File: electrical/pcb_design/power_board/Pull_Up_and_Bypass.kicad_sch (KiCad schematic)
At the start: 22 parts

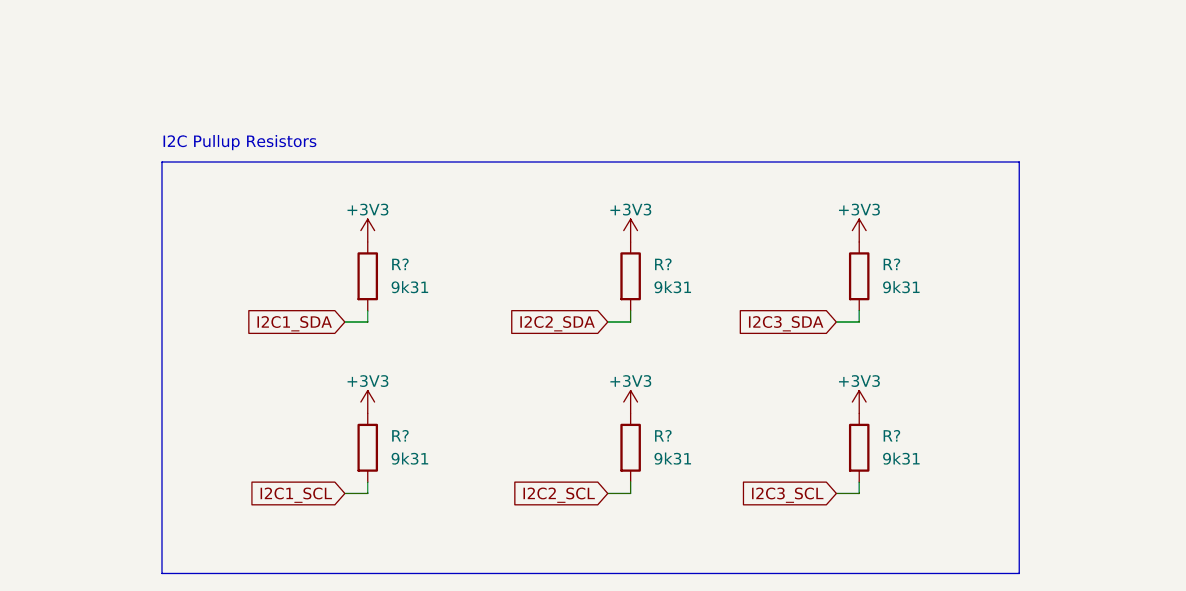
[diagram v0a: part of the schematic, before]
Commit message: power board schematic first draft but missing some resistor and diode specs, and smart mcu pinout
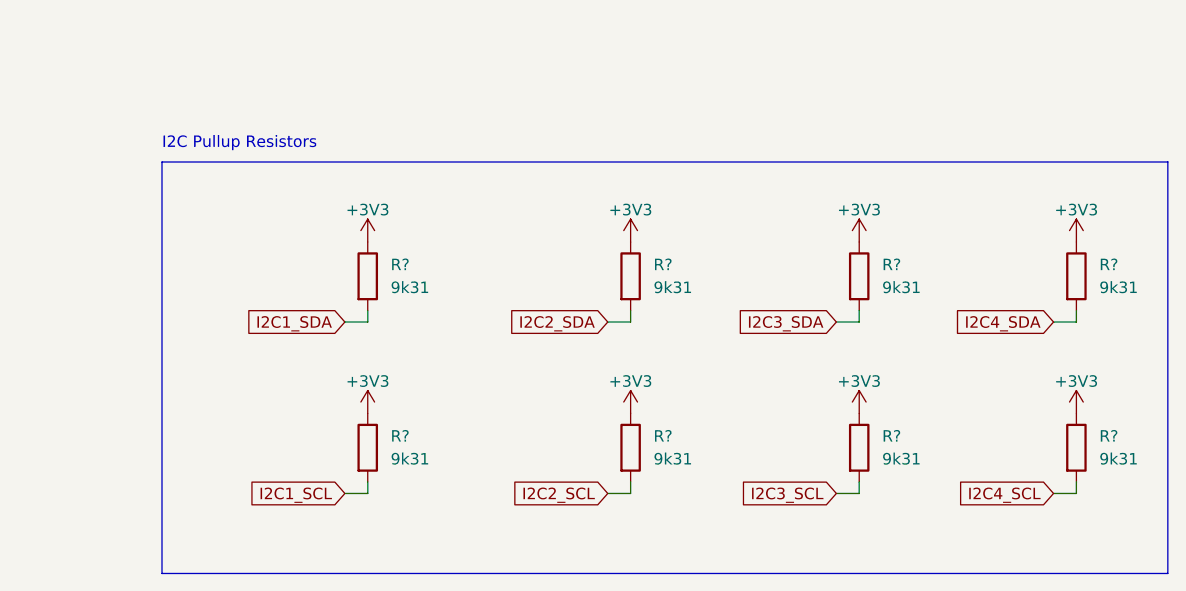
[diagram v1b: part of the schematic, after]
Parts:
- added R? (x2): 9k31, footprints:Nondescript_R_0402_1005Metric, symbol Device:R
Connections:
- net +3V3: now also R?.1, R?.1
- new net I2C4_SCL: R?.2
- new net I2C4_SDA: R?.2
